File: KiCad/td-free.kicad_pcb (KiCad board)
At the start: 2 copper layers, 60 x 30 mm, 19 parts, among them J1 Conn_01x02_Pin, J2 USB_C_Receptacle_USB2.0_14P, Q1 2N7002, U1 ESP32-C3-WROOM-02, U2 VEML7700-TT, U3 AMS1117-3.3, U4 VEML3328, U5 TPD4E05U06DQA

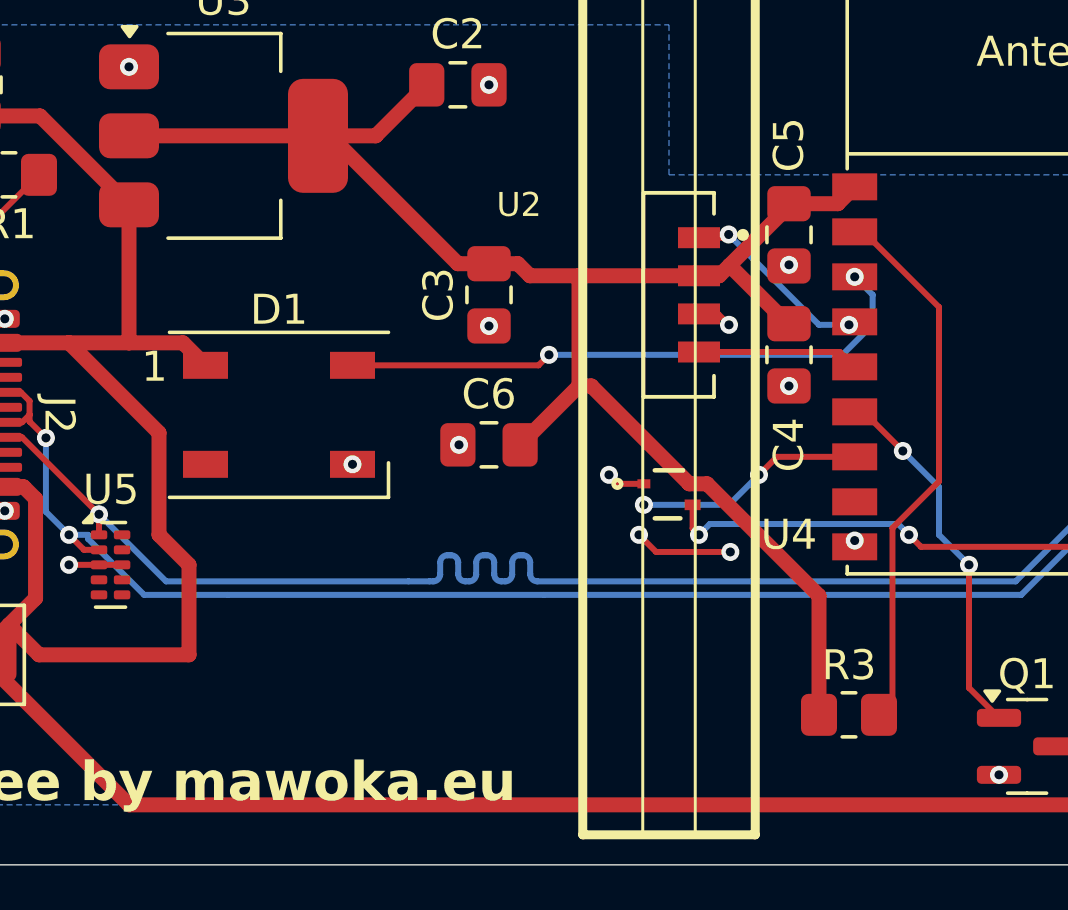
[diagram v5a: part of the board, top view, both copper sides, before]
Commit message: :sparkles: New PCB working, software backwards compatible
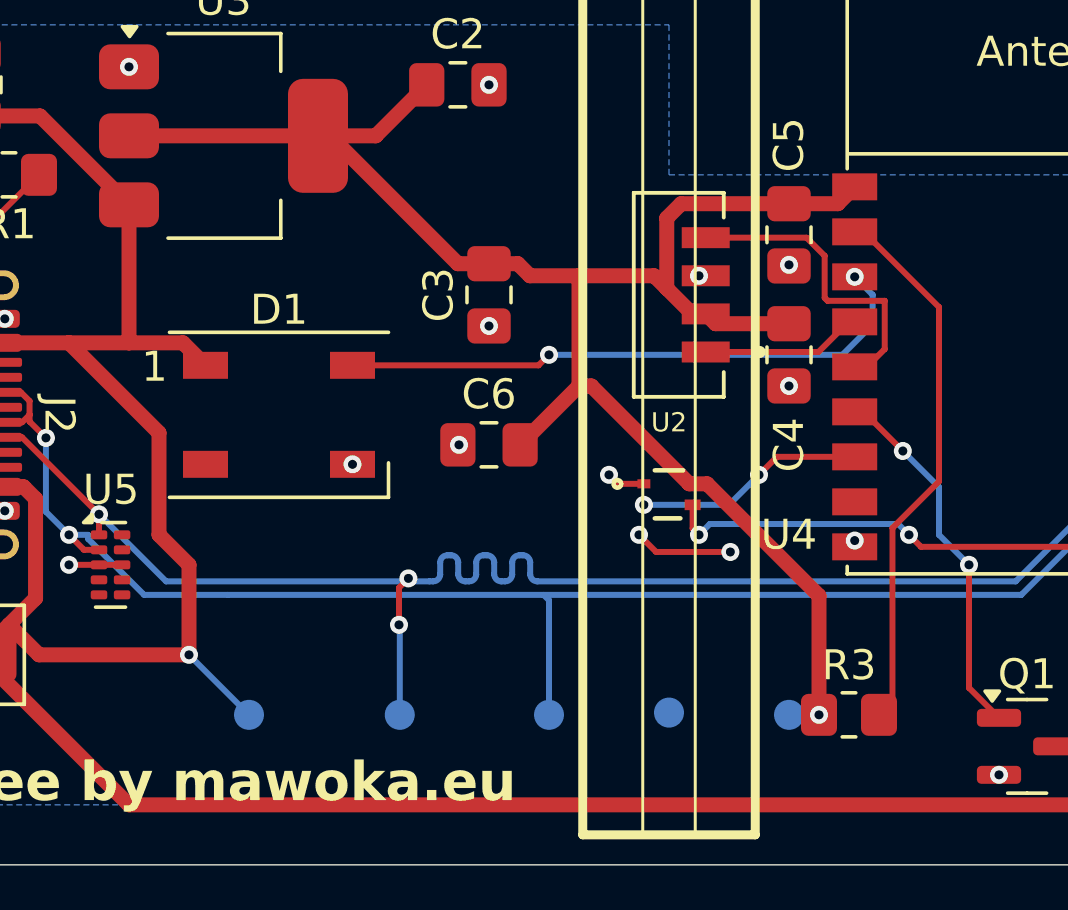
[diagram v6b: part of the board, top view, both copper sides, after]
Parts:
- added TP1: +3V3, TestPoint:TestPoint_Pad_D1.0mm, B.Cu at (48.0, 40.0)
- added TP2: GND, TestPoint:TestPoint_Pad_D1.0mm, B.Cu at (44.0, 39.9)
- added TP3: USB-, TestPoint:TestPoint_Pad_D1.0mm, B.Cu at (40.0, 40.0)
- added TP4: USB+, TestPoint:TestPoint_Pad_D1.0mm, B.Cu at (35.0, 40.0)
- added TP5: USB+, TestPoint:TestPoint_Pad_D1.0mm, B.Cu at (30.0, 40.0)
- U2: footprint VEML7700_TR:XDCR_VEML7700-TR -> VEML7700_TR:XDCR_VEML7700-TT
- turned U2 to 180 degrees
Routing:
- net +3V3: track 55.8 -> 61.0 mm, vias 0 -> 1
- net /SDA2: track 5.40 -> 10.5 mm
- net /USB_D+: track 57.9 -> 62.6 mm, vias 2 -> 4
- net /USB_D-: track 55.8 -> 59.9 mm
- net VBUS: track 108.5 -> 111.4 mm, vias 0 -> 1
- net /SCL2: track 6.39 -> 5.38 mm, vias 2 -> 0
